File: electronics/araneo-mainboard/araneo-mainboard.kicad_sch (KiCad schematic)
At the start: 82 parts, among them IC1 TPS54302DDCR, J2 OLED, J3 GPIO, SW2 SW, SW3 SW, U4 POWER, U5 PAM8403D, U6 3V3

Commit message: electronics: change capacitor footprint
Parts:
- C41: footprint Capacitor_SMD:C_0603_1608Metric_Pad1.08x0.95mm_HandSolder -> Capacitor_SMD:C_0805_2012Metric_Pad1.18x1.45mm_HandSolder
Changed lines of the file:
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@@
 			)
 		)
-		(property "Footprint" "Capacitor_SMD:C_0603_1608Metric_Pad1.08x0.95mm_HandSolder"
+		(property "Footprint" "Capacitor_SMD:C_0805_2012Metric_Pad1.18x1.45mm_HandSolder"
 			(at 239.7252 58.42 0)
 			(hide yes)

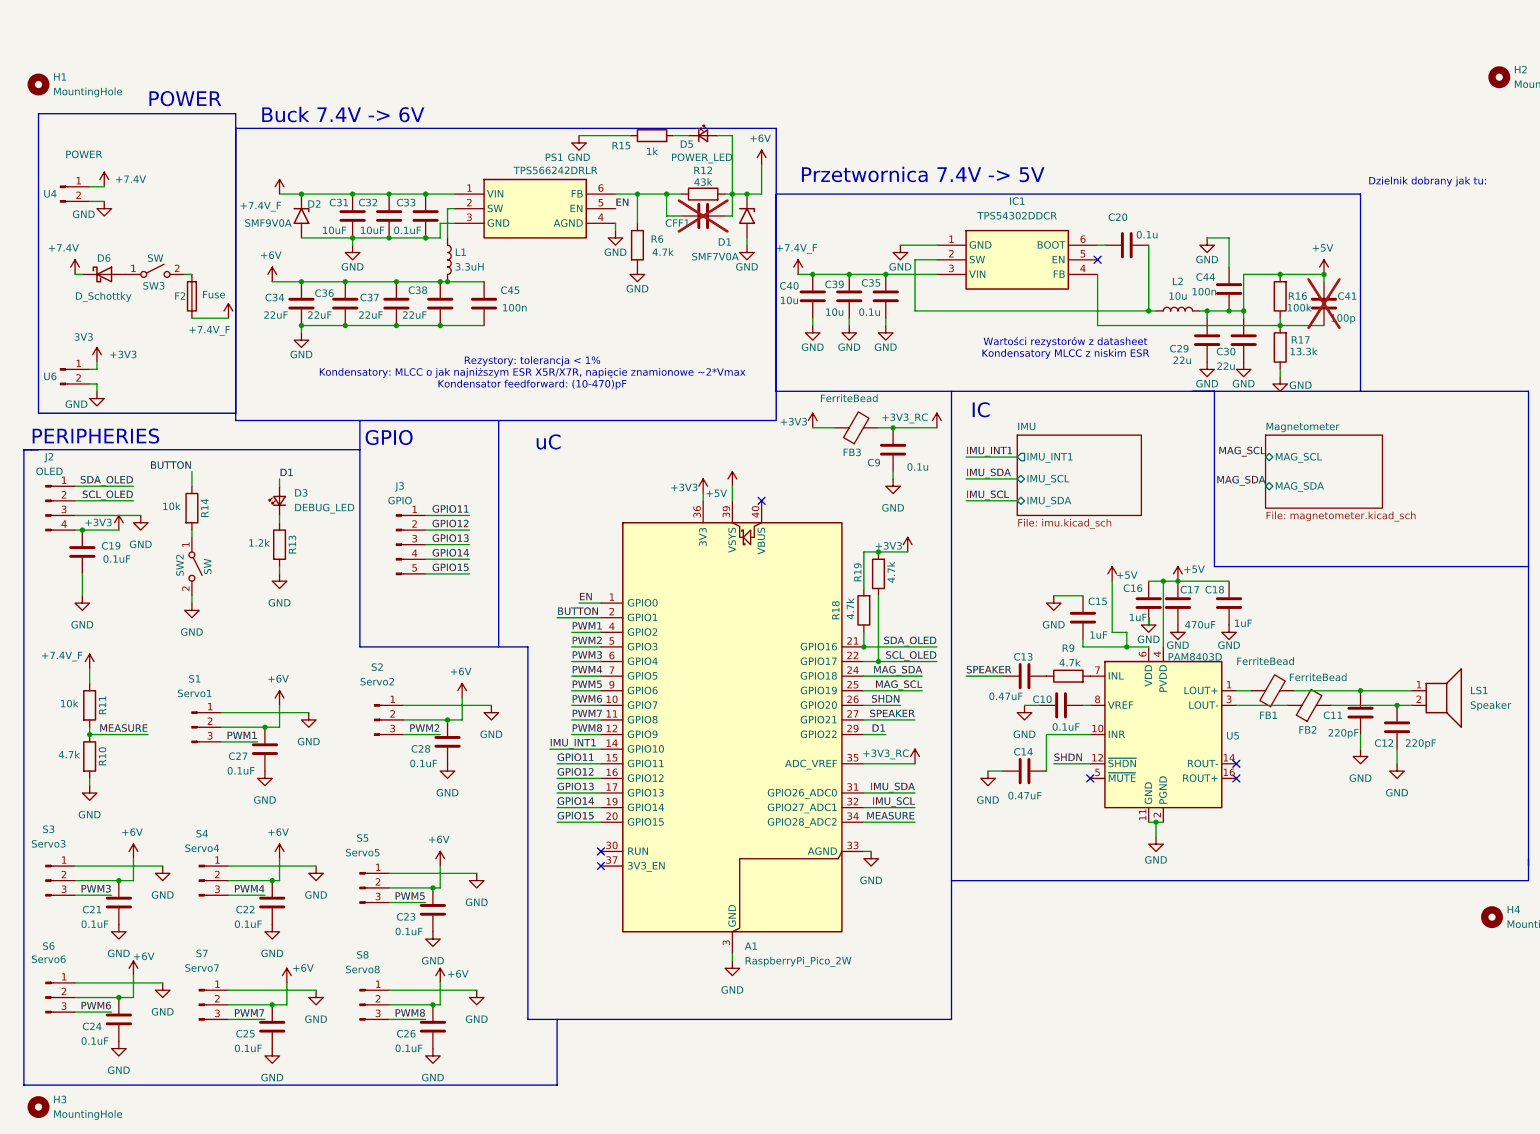
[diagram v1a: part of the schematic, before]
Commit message: electronics: remove unnecessary capacitors, add net labels, change screw terminal to JST_XH
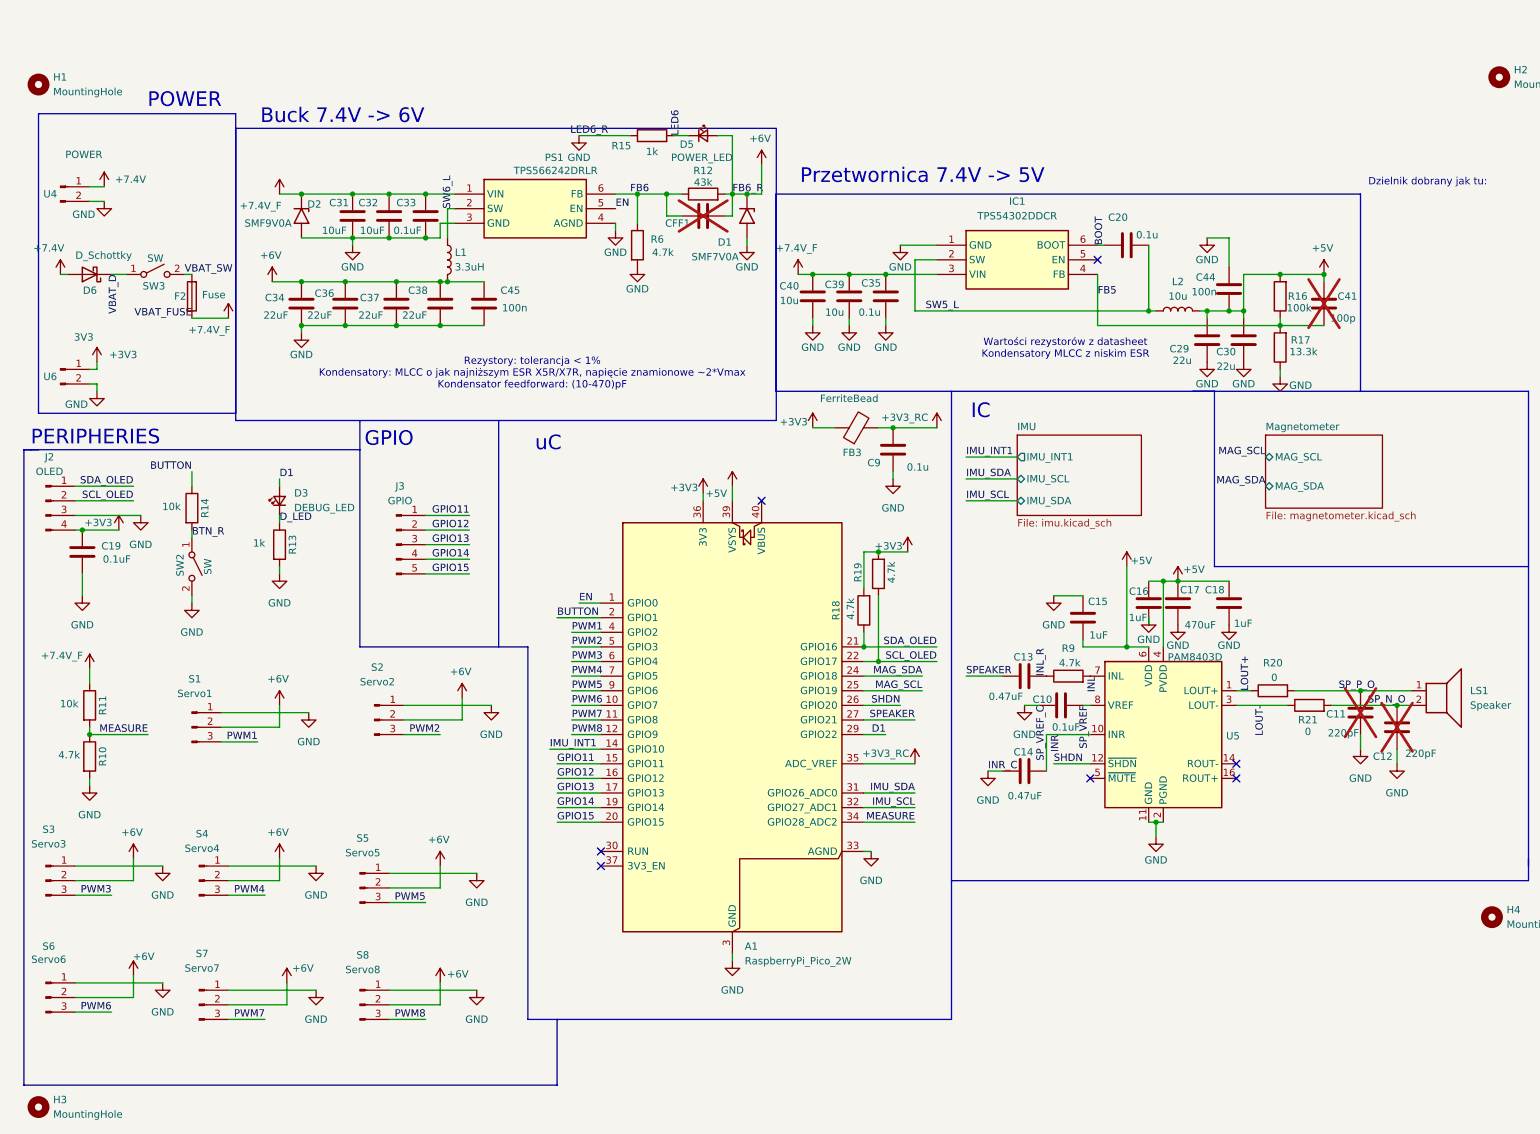
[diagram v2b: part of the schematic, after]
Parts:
- removed C21, C22, C23, C24, C25, C26, C27, C28: 0.1uF, Capacitor_SMD:C_0603_1608Metric_Pad1.08x0.95mm_HandSolder, symbol Device:C
- removed FB1, FB2: FerriteBead, Resistor_SMD:R_0603_1608Metric_Pad0.98x0.95mm_HandSolder, symbol Device:FerriteBead
- added R20, R21: 0, Resistor_SMD:R_0603_1608Metric_Pad0.98x0.95mm_HandSolder, symbol Device:R
- C11, C12: now not fitted
- J2: footprint PCM_SparkFun-Connector:ScrewTerminal_1x04_P3.5mm_Locking -> Connector_JST:JST_XH_B4B-XH-A_1x04_P2.50mm_Vertical
- R13: value 1.2k -> 1k
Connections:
- net +7.4V: now also D6.2 (A); no longer D6.1 (K)
- net SP_VREF: now reaches C10.2, U5.8 (VREF)
- net VBAT_SW: now reaches F2.2, SW3.2 (B)
- net LOUT+: now reaches U5.1 (LOUT+)
- net LOUT+: now also R20.1
- net SP_P_O: now reaches C11.2, LS1.1
- net SP_P_O: now also R20.2
- net LED6: now reaches D5.1 (K), R15.2
- net INR: now reaches C14.2, U5.10 (INR)
- net LOUT-: now reaches U5.3 (LOUT-)
- net LOUT-: now also R21.1
- net FB6: now reaches CFF1.1, PS1.6 (FB), R12.1, R6.1
- net D_LED: now reaches D3.1 (K), R13.1
- net INL_R: now reaches C13.2, R9.1
- net VBAT_D: now reaches SW3.1 (A)
- net VBAT_D: now also D6.1 (K); no longer D6.2 (A)
- net SP_N_O: now reaches C12.2, LS1.2
- net SP_N_O: now also R21.2
- net SW5_L: now reaches C20.1, IC1.2 (SW), L2.1
- net SW6_L: now reaches L1.1, PS1.2 (SW)
- net BOOT: now reaches C20.2, IC1.6 (BOOT)
- net FB5: now reaches C41.2, IC1.4 (FB), R16.1, R17.2
- net BTN_R: now reaches R14.2, SW2.1 (A)
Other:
- moved on the sheet: D6

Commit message: electronics: change bucks layout
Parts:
- added C1, C42, C5: 0.1u, Capacitor_SMD:C_0603_1608Metric_Pad1.08x0.95mm_HandSolder, symbol Device:C
- added C2: 10u, Capacitor_SMD:C_1206_3216Metric_Pad1.33x1.80mm_HandSolder, symbol Device:C
- added C3, C4, C43: 1u, Capacitor_SMD:C_0603_1608Metric_Pad1.08x0.95mm_HandSolder, symbol Device:C
- added FB4: FerriteBead, Resistor_SMD:R_0603_1608Metric_Pad0.98x0.95mm_HandSolder, symbol Device:FerriteBead
- added IC2: BMI270, custom_footprints:BMI270, symbol Symbols:BMI270
- added IC3: MMC5983MA, custom_footprints:MMC5983MA, symbol Symbols:MMC5983MA
- added R1, R2, R3, R4: 4.7k, Resistor_SMD:R_0603_1608Metric_Pad0.98x0.95mm_HandSolder, symbol Device:R
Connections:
- net +3V3: now also C1.2, C3.2, C4.2, C5.2, FB4.2, IC2.12 (CSB), IC2.5 (VDDIO), IC3.13 (VDDIO), IC3.2 (VDD), IC3.4 (SPI_CS), R1.1, R2.1, R3.2, R4.2
- net GND: now also C1.1, C2.2, C3.1, C4.1, C42.1, C43.1, C5.1, IC2.1 (SDO), IC2.6 (GNDIO), IC2.7 (GND), IC3.11 (GND_2), IC3.9 (GND_1)
- net IMU_INT1: now also IC2.4 (INT1)
- net IMU_SCL: now also IC2.13 (SCX), R1.2
- net IMU_SDA: now also IC2.14 (SDX), R2.2
- net INL: now also R9.2, U5.7 (INL)
- net MAG_SCL: now also IC3.1 (SCL/SPI_SCK), R3.1
- net MAG_SDA: now also IC3.16 (SDA/SPI_SDI), R4.1
- new net MAG_CAP: C2.1, IC3.10 (CAP)
- new net VDD_IMU: C42.2, C43.2, FB4.1, IC2.8 (VDD)
- no-connect marks 7 -> 20
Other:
- removed sheet IMU
- removed sheet Magnetometer
- note added: "IMU"
- note added: "MAGNETOMETER"
- note removed: "IC"
- moved on the sheet: A1, C10, C11, C12, C13, C14, C15, C16, C17, C18, C9, FB3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

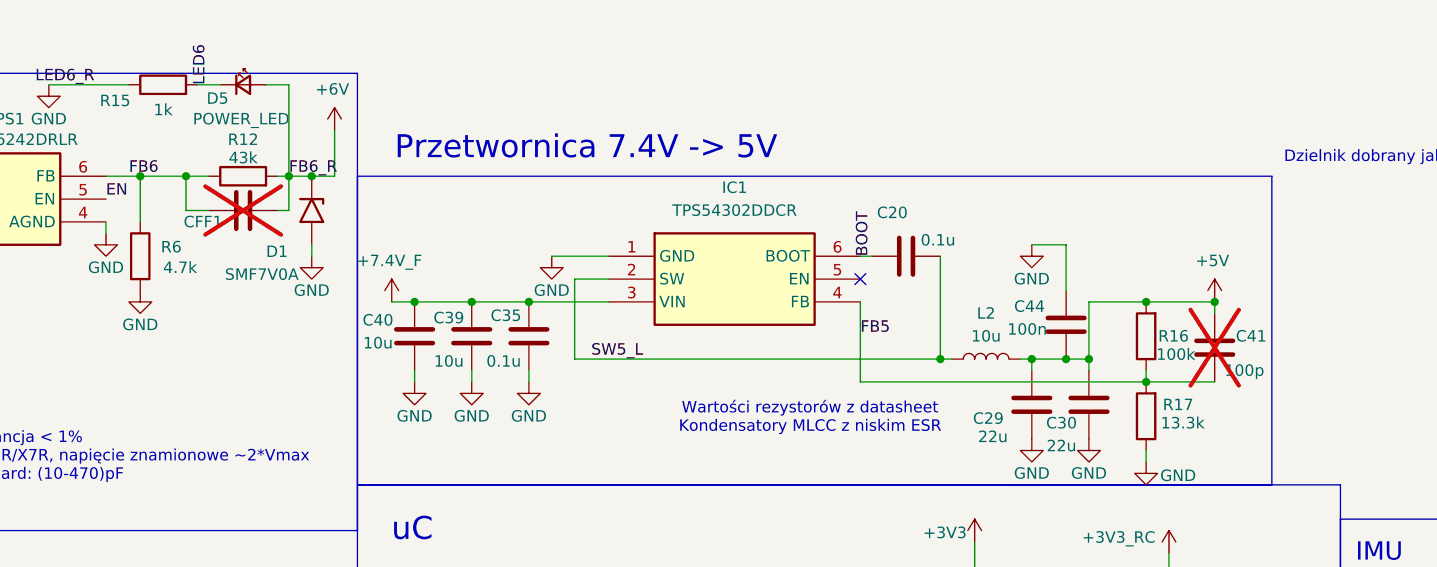
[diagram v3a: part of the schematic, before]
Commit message: electronics: change buck layout
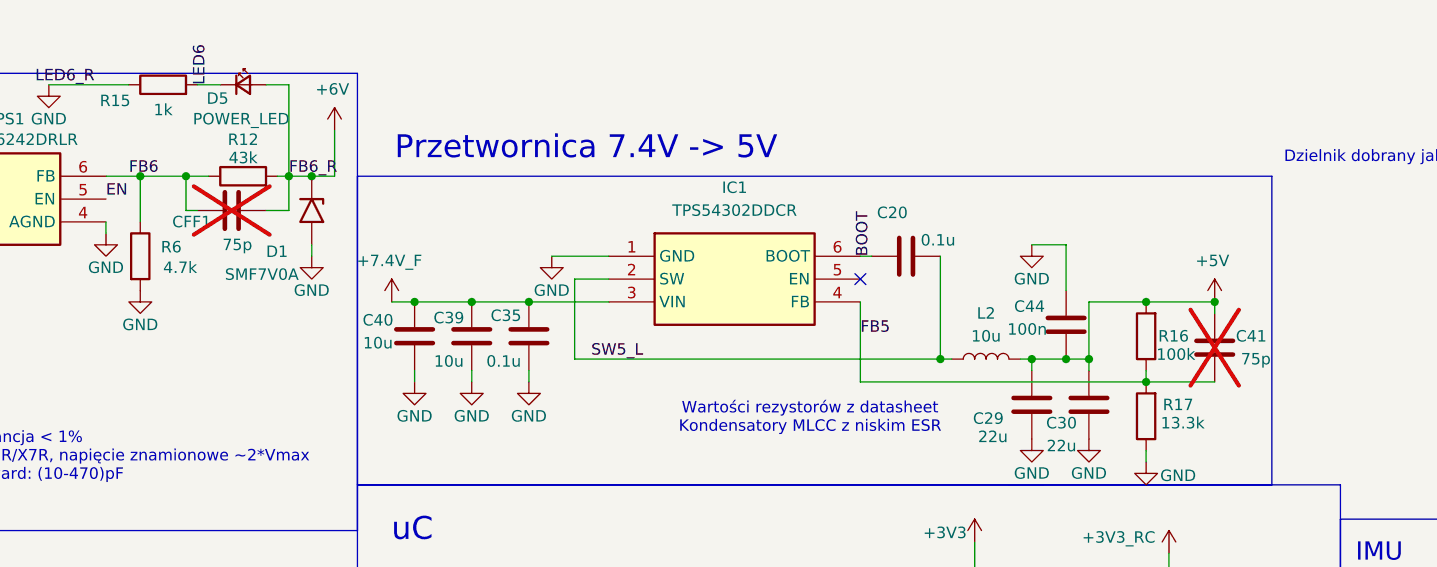
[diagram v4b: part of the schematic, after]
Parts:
- C2, C31, C32, C39, C40: footprint Capacitor_SMD:C_1206_3216Metric_Pad1.33x1.80mm_HandSolder -> Capacitor_SMD:C_0603_1608Metric_Pad1.08x0.95mm_HandSolder
- C29, C30, C34, C36, C37, C38: footprint Capacitor_SMD:C_0805_2012Metric_Pad1.18x1.45mm_HandSolder -> Capacitor_SMD:C_0603_1608Metric_Pad1.08x0.95mm_HandSolder
- C41: value 100p -> 75p; footprint Capacitor_SMD:C_0805_2012Metric_Pad1.18x1.45mm_HandSolder -> Capacitor_SMD:C_0603_1608Metric_Pad1.08x0.95mm_HandSolder
- CFF1: value 100nF -> 75p
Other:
- moved on the sheet: CFF1
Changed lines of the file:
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@@
 	(wire
 		(pts
-			(xy 134.62 39.37) (xy 135.89 39.37)
+			(xy 133.35 39.37) (xy 135.89 39.37)
 		)
 		(stroke
@@
 	(wire
 		(pts
-			(xy 127 39.37) (xy 124.46 39.37)
+			(xy 125.73 39.37) (xy 124.46 39.37)
 		)
 		(stroke
@@
 			)
 		)
-		(property "Footprint" "Capacitor_SMD:C_0805_2012Metric_Pad1.18x1.45mm_HandSolder"
+		(property "Footprint" "Capacitor_SMD:C_0603_1608Metric_Pad1.08x0.95mm_HandSolder"
 			(at 61.9252 58.42 0)
 			(hide yes)
@@
 			)
 		)
-		(property "Footprint" "Capacitor_SMD:C_0805_2012Metric_Pad1.18x1.45mm_HandSolder"
+		(property "Footprint" "Capacitor_SMD:C_0603_1608Metric_Pad1.08x0.95mm_HandSolder"
 			(at 219.4052 64.77 0)
 			(hide yes)
@@
 	(symbol
 		(lib_id "Device:C")
-		(at 130.81 39.37 90)
+		(at 129.54 39.37 90)
 		(unit 1)
 		(body_style 1)
@@
 		(dnp yes)
 		(property "Reference" "CFF1"
-			(at 128.524 40.64 90)
+			(at 127.254 40.64 90)
 			(show_name no)
 			(do_not_autoplace no)
@@
 			)
 		)
-		(property "Value" "100nF"
-			(at 138.938 41.91 90)
-			(hide yes)
+		(property "Value" "75p"
+			(at 131.826 43.18 90)
 			(show_name no)
 			(do_not_autoplace no)
@@
 		)
 		(property "Footprint" "Capacitor_SMD:C_0603_1608Metric_Pad1.08x0.95mm_HandSolder"
-			(at 134.62 38.4048 0)
+			(at 133.35 38.4048 0)
 			(hide yes)
 			(show_name no)
@@
 		)
 		(property "Datasheet" ""
-			(at 130.81 39.37 0)
+			(at 129.54 39.37 0)
 			(hide yes)
 			(show_name no)
@@
 		)
 		(property "Description" "Unpolarized capacitor"
-			(at 130.81 39.37 0)
+			(at 129.54 39.37 0)
 			(hide yes)
 			(show_name no)
@@
 			)
 		)
-		(property "Footprint" "Capacitor_SMD:C_1206_3216Metric_Pad1.33x1.80mm_HandSolder"
+		(property "Footprint" "Capacitor_SMD:C_0603_1608Metric_Pad1.08x0.95mm_HandSolder"
 			(at 70.8152 43.18 0)
 			(hide yes)
@@
 			)
 		)
-		(property "Footprint" "Capacitor_SMD:C_1206_3216Metric_Pad1.33x1.80mm_HandSolder"
+		(property "Footprint" "Capacitor_SMD:C_0603_1608Metric_Pad1.08x0.95mm_HandSolder"
 			(at 355.2952 154.94 0)
 			(hide yes)
@@
 			)
 		)
-		(property "Footprint" "Capacitor_SMD:C_0805_2012Metric_Pad1.18x1.45mm_HandSolder"
+		(property "Footprint" "Capacitor_SMD:C_0603_1608Metric_Pad1.08x0.95mm_HandSolder"
 			(at 69.5452 58.42 0)
 			(hide yes)
@@
 			)
 		)
-		(property "Footprint" "Capacitor_SMD:C_0805_2012Metric_Pad1.18x1.45mm_HandSolder"
+		(property "Footprint" "Capacitor_SMD:C_0603_1608Metric_Pad1.08x0.95mm_HandSolder"
 			(at 225.7552 64.77 0)
 			(hide yes)
@@
 			)
 		)
-		(property "Footprint" "Capacitor_SMD:C_0805_2012Metric_Pad1.18x1.45mm_HandSolder"
+		(property "Footprint" "Capacitor_SMD:C_0603_1608Metric_Pad1.08x0.95mm_HandSolder"
 			(at 86.0552 58.42 0)
 			(hide yes)
@@
 			)
 		)
-		(property "Footprint" "Capacitor_SMD:C_0805_2012Metric_Pad1.18x1.45mm_HandSolder"
+		(property "Footprint" "Capacitor_SMD:C_0603_1608Metric_Pad1.08x0.95mm_HandSolder"
 			(at 78.4352 58.42 0)
 			(hide yes)
@@
 			)
 		)
-		(property "Footprint" "Capacitor_SMD:C_1206_3216Metric_Pad1.33x1.80mm_HandSolder"
+		(property "Footprint" "Capacitor_SMD:C_0603_1608Metric_Pad1.08x0.95mm_HandSolder"
 			(at 157.1752 57.15 0)
 			(hide yes)
@@
 			)
 		)
-		(property "Footprint" "Capacitor_SMD:C_1206_3216Metric_Pad1.33x1.80mm_HandSolder"
+		(property "Footprint" "Capacitor_SMD:C_0603_1608Metric_Pad1.08x0.95mm_HandSolder"
 			(at 150.8252 57.15 0)
 			(hide yes)
@@
 			)
 		)
-		(property "Value" "100p"
-			(at 242.062 57.15 0)
+		(property "Value" "75p"
+			(at 243.332 55.88 0)
 			(show_name no)
 			(do_not_autoplace no)
@@
 			)
 		)
-		(property "Footprint" "Capacitor_SMD:C_0805_2012Metric_Pad1.18x1.45mm_HandSolder"
+		(property "Footprint" "Capacitor_SMD:C_0603_1608Metric_Pad1.08x0.95mm_HandSolder"
 			(at 239.7252 58.42 0)
 			(hide yes)
@@
 			)
 		)
-		(property "Footprint" "Capacitor_SMD:C_1206_3216Metric_Pad1.33x1.80mm_HandSolder"
+		(property "Footprint" "Capacitor_SMD:C_0603_1608Metric_Pad1.08x0.95mm_HandSolder"
 			(at 77.1652 43.18 0)
 			(hide yes)
